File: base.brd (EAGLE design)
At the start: 49.2 x 80 mm, 6 parts

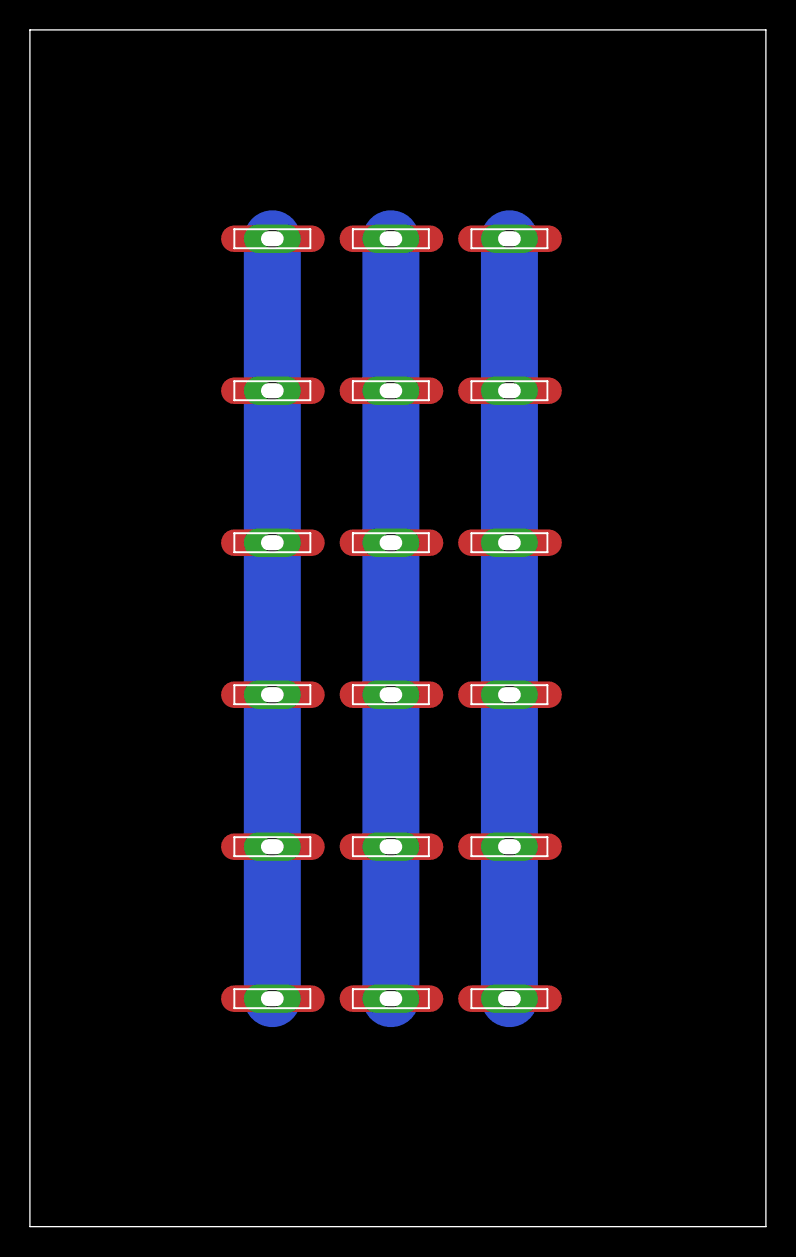
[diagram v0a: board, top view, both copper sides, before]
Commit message: split traces between top and bottom copper to reduce trace width
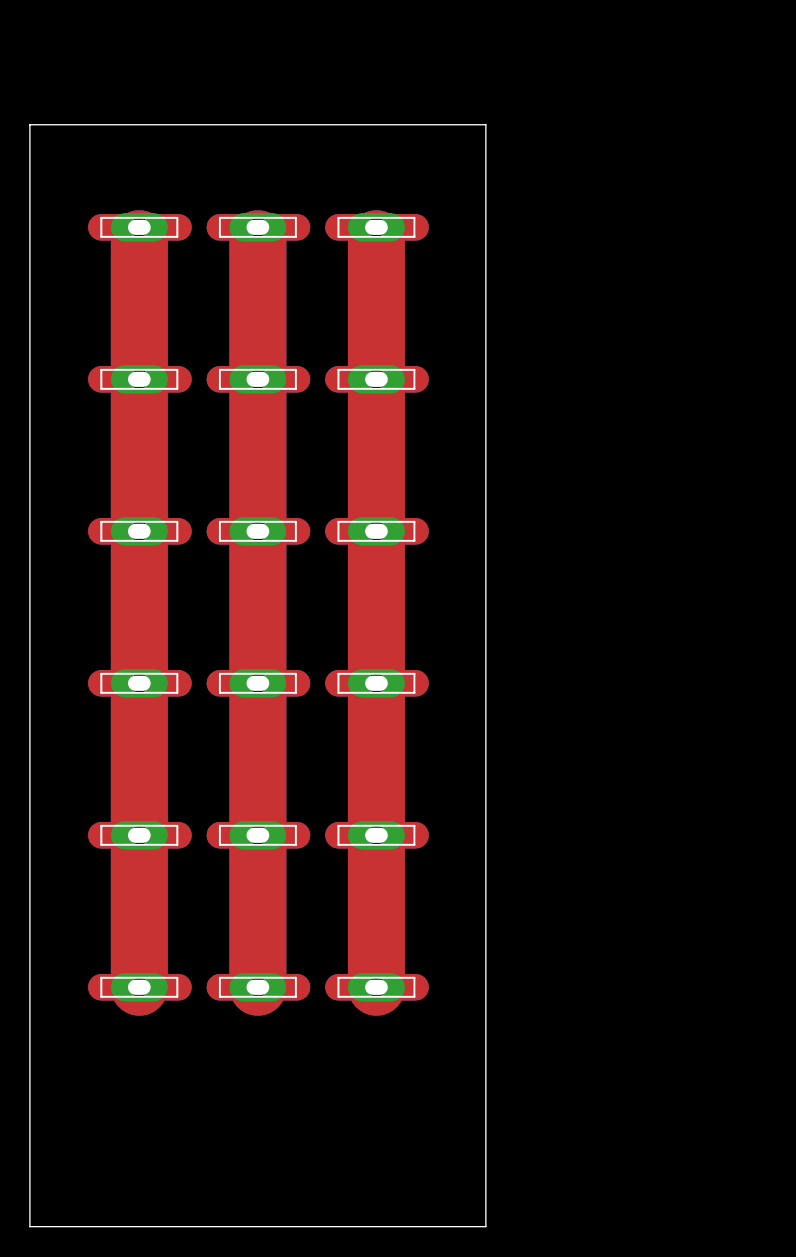
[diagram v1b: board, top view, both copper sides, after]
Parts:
- moved U$2 8.92 mm to (15.2, 26.2)
- moved U$3 8.92 mm to (15.2, 36.3)
- moved U$4 8.92 mm to (15.2, 46.5)
- moved U$5 8.92 mm to (15.2, 56.6)
- moved U$6 8.92 mm to (15.2, 66.8)
- moved U$1 8.92 mm to (15.2, 16.0)
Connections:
- net N$1 renamed GND
- net N$3 renamed 5V
- removed net N$4: U$1.3V, U$2.3V, U$3.3V, U$4.3V, U$5.3V, U$6.3V
- new net 12V: U$1.12V, U$2.12V, U$3.12V, U$4.12V, U$5.12V, U$6.12V
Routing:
- net 12V: track 0.00 -> 94.0 mm
- net N$4: track 50.8 -> 0.00 mm
- net 5V: track 50.8 -> 97.0 mm
- net GND: track 50.8 -> 94.0 mm
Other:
- board size 49.2 x 80 mm -> 30.5 x 73.7 mm
- board text added: "12V"
- board text added: "5V"
- board text added: "GND"
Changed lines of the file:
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@@
 <setting verticaltext="up"/>
 </settings>
-<grid distance="0.4" unitdist="inch" unit="inch" style="lines" multiple="1" display="yes" altdistance="0.025" altunitdist="inch" altunit="inch"/>
+<grid distance="0.2" unitdist="inch" unit="inch" style="lines" multiple="1" display="yes" altdistance="0.025" altunitdist="inch" altunit="inch"/>
 <layers>
 <layer number="1" name="Top" color="4" fill="1" visible="yes" active="yes"/>
@@
 <board>
 <plain>
-<wire x1="0" y1="0" x2="49.2" y2="0" width="0" layer="20"/>
-<wire x1="49.2" y1="0" x2="49.2" y2="80" width="0" layer="20"/>
-<wire x1="49.2" y1="80" x2="0" y2="80" width="0" layer="20"/>
-<wire x1="0" y1="80" x2="0" y2="0" width="0" layer="20"/>
+<wire x1="0" y1="0" x2="30.48" y2="0" width="0" layer="20"/>
+<wire x1="30.48" y1="0" x2="30.48" y2="73.66" width="0" layer="20"/>
+<wire x1="30.48" y1="73.66" x2="0" y2="73.66" width="0" layer="20"/>
+<wire x1="0" y1="73.66" x2="0" y2="0" width="0" layer="20"/>
+<text x="7.62" y="7.62" size="2.54" layer="26" font="fixed" align="center">GND</text>
+<text x="15.24" y="7.62" size="2.54" layer="26" font="fixed" align="center">5V</text>
+<text x="22.86" y="7.62" size="2.54" layer="26" font="fixed" align="center">12V</text>
 </plain>
 <attributes>
@@
 <classes>
 <class number="0" name="default" width="0" drill="0">
+</class>
+<class number="1" name="Vcc" width="3.6068" drill="0.381">
+<clearance class="1" value="0.254"/>
 </class>
 </classes>
@@
 <autorouter>
 <pass name="Default">
-<param name="RoutingGrid" value="50mil"/>
+<param name="RoutingGrid" value="12.5mil"/>
 <param name="AutoGrid" value="1"/>
 <param name="Efforts" value="0"/>
 <param name="TopRouterVariant" value="1"/>
 <param name="tpViaShape" value="round"/>
-<param name="PrefDir.1" value="a"/>
+<param name="PrefDir.1" value="|"/>
 <param name="PrefDir.2" value="0"/>
 <param name="PrefDir.3" value="0"/>
@@
 <param name="PrefDir.14" value="0"/>
 <param name="PrefDir.15" value="0"/>
-<param name="PrefDir.16" value="a"/>
+<param name="PrefDir.16" value="-"/>
 <param name="cfVia" value="8"/>
 <param name="cfNonPref" value="5"/>
@@
 </autorouter>
 <elements>
-<element name="U$1" library="jack" package="ARC2" value="3POLE" x="24.13" y="15.24"/>
-<element name="U$2" library="jack" package="ARC2" value="3POLE" x="24.13" y="25.4"/>
-<element name="U$3" library="jack" package="ARC2" value="3POLE" x="24.13" y="35.56"/>
-<element name="U$4" library="jack" package="ARC2" value="3POLE" x="24.13" y="45.72"/>
-<element name="U$5" library="jack" package="ARC2" value="3POLE" x="24.13" y="55.88"/>
-<element name="U$6" library="jack" package="ARC2" value="3POLE" x="24.13" y="66.04"/>
+<element name="U$1" library="jack" package="ARC2" value="3POLE" x="15.24" y="16.002"/>
+<element name="U$2" library="jack" package="ARC2" value="3POLE" x="15.24" y="26.162"/>
+<element name="U$3" library="jack" package="ARC2" value="3POLE" x="15.24" y="36.322"/>
+<element name="U$4" library="jack" package="ARC2" value="3POLE" x="15.24" y="46.482"/>
+<element name="U$5" library="jack" package="ARC2" value="3POLE" x="15.24" y="56.642"/>
+<element name="U$6" library="jack" package="ARC2" value="3POLE" x="15.24" y="66.802"/>
 </elements>
 <signals>
-<signal name="N$1">
-<contactref element="U$1" pad="GND"/>
+<signal name="GND">
 <contactref element="U$2" pad="GND"/>
 <contactref element="U$5" pad="GND"/>
@@
 <contactref element="U$4" pad="GND"/>
 <contactref element="U$6" pad="GND"/>
-<wire x1="16.2052" y1="66.04" x2="16.2052" y2="15.24" width="3.81" layer="16"/>
-<wire x1="16.2052" y1="45.72" x2="16.2052" y2="55.88" width="0" layer="19" extent="1-1"/>
-<wire x1="16.2052" y1="35.56" x2="16.2052" y2="45.72" width="0" layer="19" extent="1-1"/>
-<wire x1="16.2052" y1="25.4" x2="16.2052" y2="35.56" width="0" layer="19" extent="1-1"/>
-<wire x1="16.2052" y1="66.04" x2="16.2052" y2="55.88" width="0" layer="19" extent="1-1"/>
+<contactref element="U$1" pad="GND"/>
+<wire x1="7.3152" y1="16.002" x2="7.3152" y2="25.4" width="3.81" layer="16"/>
+<wire x1="7.3152" y1="25.4" x2="4.7752" y2="26.162" width="0" layer="19" extent="1-16"/>
+<wire x1="7.3152" y1="26.162" x2="7.3152" y2="35.56" width="3.81" layer="16"/>
+<wire x1="7.3152" y1="35.56" x2="4.7752" y2="36.322" width="0" layer="19" extent="1-16"/>
+<wire x1="7.3152" y1="36.322" x2="7.3152" y2="45.72" width="3.81" layer="16"/>
+<wire x1="7.3152" y1="45.72" x2="4.7752" y2="46.482" width="0" layer="19" extent="1-16"/>
+<wire x1="7.3152" y1="46.482" x2="7.3152" y2="55.88" width="3.81" layer="16"/>
+<wire x1="7.3152" y1="55.88" x2="4.7752" y2="56.642" width="0" layer="19" extent="1-16"/>
+<wire x1="7.3152" y1="56.642" x2="7.3152" y2="66.04" width="3.81" layer="16"/>
+<wire x1="7.3152" y1="66.04" x2="4.7752" y2="66.802" width="0" layer="19" extent="1-16"/>
+<wire x1="7.3152" y1="16.002" x2="7.3152" y2="25.4" width="3.81" layer="1"/>
+<wire x1="7.3152" y1="26.162" x2="7.3152" y2="35.56" width="3.81" layer="1"/>
+<wire x1="7.3152" y1="36.322" x2="7.3152" y2="45.72" width="3.81" layer="1"/>
+<wire x1="7.3152" y1="46.482" x2="7.3152" y2="55.88" width="3.81" layer="1"/>
+<wire x1="7.3152" y1="56.642" x2="7.3152" y2="66.04" width="3.81" layer="1"/>
 </signal>
-<signal name="N$3">
+<signal name="12V">
+<contactref element="U$2" pad="12V"/>
+<contactref element="U$5" pad="12V"/>
+<contactref element="U$1" pad="12V"/>
+<contactref element="U$3" pad="12V"/>
+<contactref element="U$6" pad="12V"/>
+<contactref element="U$4" pad="12V"/>
+<wire x1="23.1648" y1="16.002" x2="23.1648" y2="25.4" width="3.81" layer="16"/>
+<wire x1="23.1648" y1="25.4" x2="25.781" y2="26.162" width="0" layer="19" extent="1-16"/>
+<wire x1="23.1648" y1="26.162" x2="23.1648" y2="35.56" width="3.81" layer="16"/>
+<wire x1="23.1648" y1="35.56" x2="25.781" y2="36.322" width="0" layer="19" extent="1-16"/>
+<wire x1="23.1648" y1="36.322" x2="23.1648" y2="45.72" width="3.81" layer="16"/>
+<wire x1="23.1648" y1="45.72" x2="25.781" y2="46.482" width="0" layer="19" extent="1-16"/>
+<wire x1="23.1648" y1="46.482" x2="23.1648" y2="55.88" width="3.81" layer="16"/>
+<wire x1="23.1648" y1="55.88" x2="25.781" y2="56.642" width="0" layer="19" extent="1-16"/>
+<wire x1="23.1648" y1="56.642" x2="23.1648" y2="66.04" width="3.81" layer="16"/>
+<wire x1="23.1648" y1="66.04" x2="25.781" y2="66.802" width="0" layer="19" extent="1-16"/>
+<wire x1="23.1648" y1="16.002" x2="23.1648" y2="25.4" width="3.81" layer="1"/>
+<wire x1="23.1648" y1="26.162" x2="23.1648" y2="35.56" width="3.81" layer="1"/>
+<wire x1="23.1648" y1="36.322" x2="23.1648" y2="45.72" width="3.81" layer="1"/>
+<wire x1="23.1648" y1="46.482" x2="23.1648" y2="55.88" width="3.81" layer="1"/>
+<wire x1="23.1648" y1="56.642" x2="23.1648" y2="66.04" width="3.81" layer="1"/>
+</signal>
+<signal name="5V">
+<contactref element="U$6" pad="5V"/>
+<contactref element="U$4" pad="5V"/>
+<contactref element="U$3" pad="5V"/>
+<contactref element="U$5" pad="5V"/>
+<contactref element="U$2" pad="5V"/>
 <contactref element="U$1" pad="5V"/>
-<contactref element="U$2" pad="5V"/>
-<contactref element="U$5" pad="5V"/>
-<contactref element="U$3" pad="5V"/>
-<contactref element="U$4" pad="5V"/>
-<contactref element="U$6" pad="5V"/>
-<wire x1="32.0548" y1="15.24" x2="32.0548" y2="66.04" width="3.81" layer="16"/>
-<wire x1="32.0548" y1="45.72" x2="32.0548" y2="55.88" width="0" layer="19" extent="1-1"/>
-<wire x1="32.0548" y1="35.56" x2="32.0548" y2="45.72" width="0" layer="19" extent="1-1"/>
-<wire x1="32.0548" y1="25.4" x2="32.0548" y2="35.56" width="0" layer="19" extent="1-1"/>
-<wire x1="32.0548" y1="66.04" x2="32.0548" y2="55.88" width="0" layer="19" extent="1-1"/>
-</signal>
-<signal name="N$4">
-<contactref element="U$6" pad="3V"/>
-<contactref element="U$4" pad="3V"/>
-<contactref element="U$3" pad="3V"/>
-<contactref element="U$5" pad="3V"/>
-<contactref element="U$1" pad="3V"/>
-<contactref element="U$2" pad="3V"/>
-<wire x1="24.13" y1="15.24" x2="24.13" y2="66.04" width="3.81" layer="16"/>
-<wire x1="24.13" y1="45.72" x2="24.13" y2="55.88" width="0" layer="19" extent="1-1"/>
-<wire x1="24.13" y1="35.56" x2="24.13" y2="45.72" width="0" layer="19" extent="1-1"/>
-<wire x1="24.13" y1="25.4" x2="24.13" y2="35.56" width="0" layer="19" extent="1-1"/>
-<wire x1="24.13" y1="66.04" x2="24.13" y2="55.88" width="0" layer="19" extent="1-1"/>
+<wire x1="15.24" y1="16.002" x2="15.24" y2="25.4" width="3.81" layer="16"/>
+<wire x1="15.24" y1="25.4" x2="15.24" y2="26.162" width="0" layer="19" extent="1-16"/>
+<wire x1="15.24" y1="26.162" x2="15.24" y2="36.322" width="3.81" layer="16"/>
+<wire x1="15.24" y1="36.322" x2="15.24" y2="45.72" width="3.81" layer="16"/>
+<wire x1="15.24" y1="45.72" x2="15.24" y2="46.482" width="0" layer="19" extent="1-16"/>
+<wire x1="15.24" y1="46.482" x2="15.24" y2="56.642" width="3.81" layer="16"/>
+<wire x1="15.24" y1="56.642" x2="15.24" y2="66.04" width="3.81" layer="16"/>
+<wire x1="15.24" y1="66.04" x2="15.24" y2="66.802" width="0" layer="19" extent="1-16"/>
+<wire x1="15.24" y1="16.002" x2="15.24" y2="25.4" width="3.81" layer="1"/>
+<wire x1="15.24" y1="26.162" x2="15.24" y2="45.72" width="3.81" layer="1"/>
+<wire x1="15.24" y1="46.482" x2="15.24" y2="66.04" width="3.81" layer="1"/>
 </signal>
 </signals>
-<errors>
-</errors>
 </board>
 </drawing>
